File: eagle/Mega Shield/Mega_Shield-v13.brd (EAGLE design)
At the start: 101.6 x 53.3 mm, 27 parts, among them U1 LCD-16X2SILK, U2 LCD-16X2SILK, U3 MAX232PTH

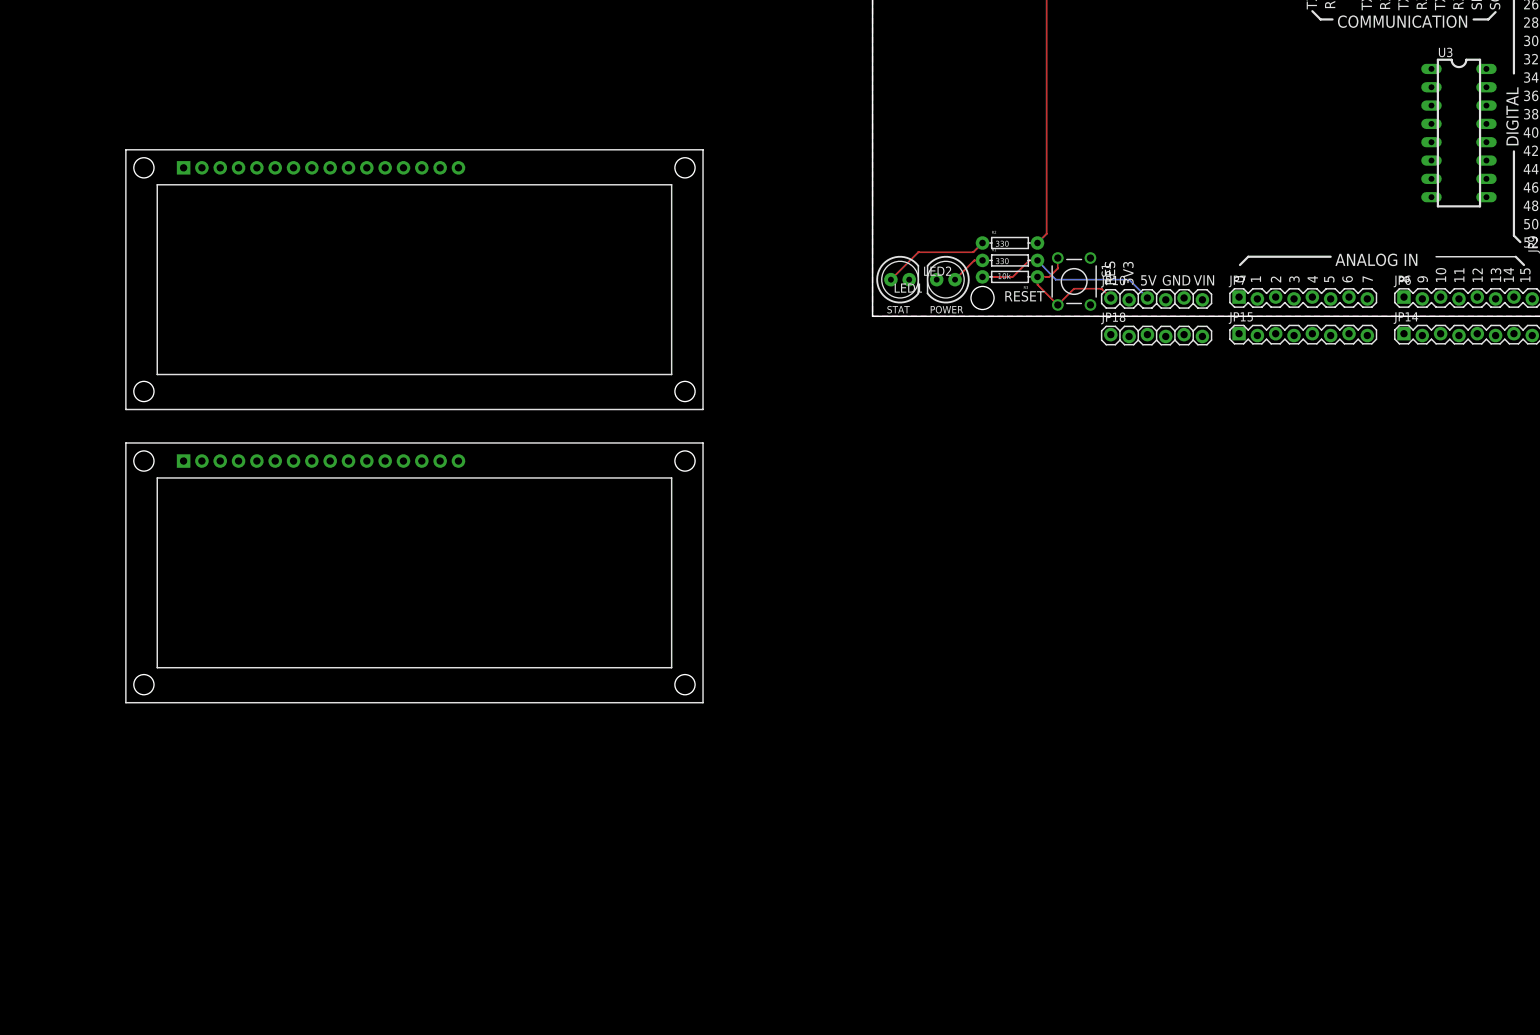
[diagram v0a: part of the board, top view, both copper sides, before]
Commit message: working on pcb, added main connector and lcds
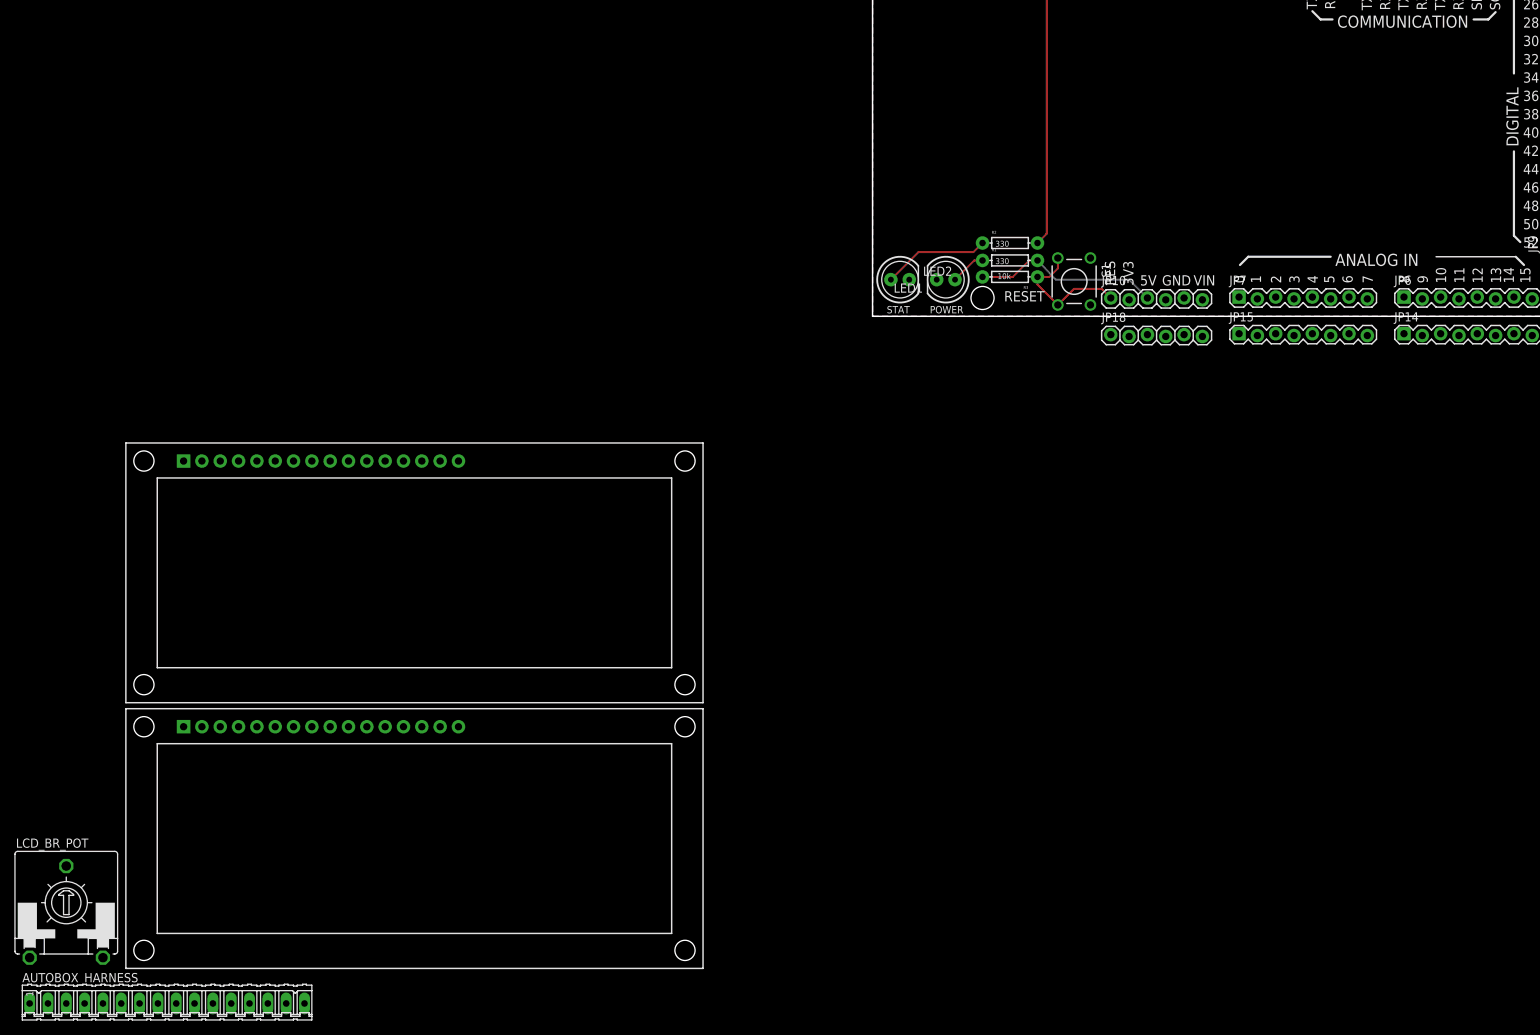
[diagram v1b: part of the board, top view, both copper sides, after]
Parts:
- removed U1: LCD-16X2SILK, SparkFun-Displays:LCD-16X2
- removed U3: MAX232PTH, SparkFun-DigitalIC:DIL16
- added AUTOBOX_HARNESS: (no value), con-amp-quick:16P
- added LCD_1: LCD-16X2SILK, SparkFun-Displays:LCD-16X2
- added LCD_BR_POT: (no value), pot:CA14V
- renumbered U2 to LCD_0
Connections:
- removed net VDD: LCD_0.2, U1.2
- removed net VSS: LCD_0.1, U1.1
- new net LCD_BR: LCD_0.3, LCD_1.3, LCD_BR_POT.S
- new net MODE0: AUTOBOX_HARNESS.8
- new net MODE1: AUTOBOX_HARNESS.9
- new net N$1: AUTOBOX_HARNESS.16
- new net N$2: AUTOBOX_HARNESS.15
- new net SERIAL_K: AUTOBOX_HARNESS.3
- new net SERIAL_L: AUTOBOX_HARNESS.4
- new net SHFT_D: AUTOBOX_HARNESS.14
- new net SHFT_U: AUTOBOX_HARNESS.13
- new net SW1: AUTOBOX_HARNESS.5
- new net SW2: AUTOBOX_HARNESS.6
- new net SW3: AUTOBOX_HARNESS.7
- new net TRC_POT: AUTOBOX_HARNESS.12
- new net TRC_SW0: AUTOBOX_HARNESS.10
- new net TRC_SW1: AUTOBOX_HARNESS.11
- net 5V: now also LCD_0.2, LCD_1.2, LCD_BR_POT.E
- net A: now also LCD_1.15; no longer U1.15
- net D22: now also LCD_0.4
- net D23: now also LCD_0.6
- net D24: now also LCD_0.11
- net D25: now also LCD_0.12
- net D26: now also LCD_0.13
- net D27: now also LCD_0.14
- net D28: now also LCD_1.4
- net D29: now also LCD_1.6
- net D30: now also LCD_1.11
- net D31: now also LCD_1.12
- net D32: now also LCD_1.13
- net D33: now also LCD_1.14
- net GND: now also AUTOBOX_HARNESS.2, LCD_0.1, LCD_0.5, LCD_1.1, LCD_1.5, LCD_BR_POT.A
- net K: now also LCD_1.16; no longer U1.16
- net VIN: now also AUTOBOX_HARNESS.1

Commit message: more changes
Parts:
- added LED3: (no value), led:LED5MM
- added Q1, Q2, Q4: 2N3904, transistor-npn:TO92
- added Q5: 2N3906, transistor-pnp:TO92
- added R10, R4, R6, R8: 10k, SparkFun-Passives:AXIAL-0.3EZ
- added R5, R7, R9: 1k, SparkFun-Passives:AXIAL-0.3EZ
- moved LCD_BR_POT 263.2 mm to (132.1, 17.8), turned to 270 degrees
- moved LCD_1 199.2 mm to (125.7, -10.2)
- moved AUTOBOX_HARNESS 174.5 mm to (5.08, 45.7), turned to 90 degrees
- moved LED1 129.3 mm to (118.1, 76.2), turned to 270 degrees
- moved R1 123.4 mm to (118.5, 80.8), turned to 180 degrees
- moved LCD_0 108.4 mm to (41.9, -10.2)
- moved LED2 71.1 mm to (40.1, 66.2)
- moved R2 59.1 mm to (47.0, 62.2)
- moved JP13 27.9 mm to (88.9, 74.9)
- moved JP1 27.9 mm to (62.2, 74.9)
- moved JP14 27.9 mm to (94.0, 16.5)
- moved JP15 27.9 mm to (71.1, 16.5)
- moved JP5 27.9 mm to (88.9, 69.8)
- moved JP6 27.9 mm to (94.0, 21.6)
- moved JP7 27.9 mm to (71.1, 21.6)
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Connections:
- new net N$10: Q4.1, R10.P$1, R8.P$1
- new net N$3: Q1.1, R4.P$1
- new net N$4: Q1.2, R5.P$1
- new net N$5: Q5.1, R5.P$2, R7.P$2
- new net N$6: Q5.2, R6.P$1
- new net N$7: LED3.A, R7.P$1
- new net N$8: Q2.2, R10.P$2
- net 5V: now also JP12.2, R4.P$2, R8.P$2
- net 5V@1: no longer JP12.2
- net D18: now also Q4.2
- net D19: now also Q1.3
- net GND: now also LED3.K, Q2.3, Q4.3
- net SERIAL_K: now also Q2.1, R6.P$2, R9.P$1
- net VIN: now also Q5.3, R9.P$2
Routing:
- net SERIAL_K: track 0.00 -> 146.7 mm
- net VIN: track 0.25 -> 79.0 mm
- net D13: track 43.4 -> 0.00 mm
- net RES: track 18.6 -> 0.00 mm
- net 5V: track 26.0 -> 7.80 mm
- net N$127: track 14.8 -> 0.00 mm
- net D29: track 0.00 -> 11.3 mm
- net D40: track 0.00 -> 11.3 mm
- net D36: track 0.00 -> 11.3 mm
- net D24: track 0.00 -> 11.3 mm
- net D52: track 0.00 -> 11.3 mm
- net D48: track 0.00 -> 11.3 mm
- net D44: track 0.00 -> 11.3 mm
- net D32: track 0.00 -> 11.3 mm
- net D28: track 0.00 -> 11.3 mm
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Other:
- board size 101.6 x 53.3 mm -> 143.5 x 95.2 mm
- board text added: "K - TX/RX"
- board text added: "LCD_0"
- board text added: "LCD_1"
- board text added: "LCD_BRIGHT"

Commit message: did a lot of pcb work
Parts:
- removed AUTOBOX_HARNESS: (no value), con-amp-quick:16P
- added ABOX_HARN, DSW_LG: (no value), Molex connectors:172064-0012
- added ABOX_PWR, DSW_SM, STEER: (no value), Molex connectors:172064-0004
- added CD4504BE: (no value), ic-package:SOCKET-16
- LCD_0, LCD_1: value LCD-16X2SILK -> 057-010-1; device SparkFun-Displays:LCD-16X2 -> con-panduit:057-010-1
- moved LCD_0 90.0 mm to (119.4, 35.6), turned to 270 degrees
- moved LCD_1 66.3 mm to (119.4, 55.9), turned to 270 degrees
- moved R4 65.9 mm to (68.6, 41.9)
- moved R1 64.8 mm to (68.6, 39.5), turned to 0 degrees
- moved R8 62.0 mm to (68.6, 44.5)
- moved LED1 61.3 mm to (73.3, 34.4), turned to 180 degrees
- moved R10 58.4 mm to (68.6, 47.0), turned to 0 degrees
- moved R6 55.0 mm to (68.6, 49.5), turned to 180 degrees
- moved LCD_BR_POT 50.4 mm to (84.5, 34.2), turned to 0 degrees
- moved Q4 49.0 mm to (68.6, 54.6), turned to 180 degrees
- moved LED3 47.3 mm to (77.5, 47.0), turned to 180 degrees
- moved R5 45.9 mm to (87.6, 44.5), turned to 0 degrees
- moved R7 40.8 mm to (87.6, 47.0), turned to 0 degrees
- moved Q2 38.7 mm to (74.9, 54.6), turned to 180 degrees
- moved R9 35.8 mm to (87.6, 49.5), turned to 0 degrees
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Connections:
- removed net 5V@1: JP12.1
- removed net A: LCD_0.15, LCD_1.15
- removed net K: LCD_0.16, LCD_1.16
- removed net N$3: Q1.1, R4.P$1
- new net N$11: CD4504BE.2
- new net N$12: CD4504BE.3
- new net N$13: CD4504BE.4
- new net N$14: CD4504BE.5
- new net N$15: CD4504BE.6
- new net N$16: CD4504BE.7
- new net N$19: CD4504BE.15
- new net N$20: CD4504BE.14
- new net N$22: CD4504BE.12
- new net N$23: CD4504BE.11
- new net N$24: CD4504BE.10
- new net N$25: CD4504BE.9
- net 5V: now also CD4504BE.1, JP12.1, LCD_0.3, LCD_1.3; no longer LCD_0.2, LCD_1.2
- net D19: now also Q1.1, R4.P$1; no longer Q1.3
- net D22: now also LCD_0.7; no longer LCD_0.4
- net D23: now also LCD_0.2; no longer LCD_0.6
- net D24: now also LCD_0.4; no longer LCD_0.11
- net D25: now also LCD_0.6; no longer LCD_0.12
- net D26: now also LCD_0.8; no longer LCD_0.13
- net D27: now also LCD_0.10; no longer LCD_0.14
- net D28: now also LCD_1.7; no longer LCD_1.4
- net D29: now also LCD_1.2; no longer LCD_1.6
- net D30: now also LCD_1.4; no longer LCD_1.11
- net D31: now also LCD_1.6; no longer LCD_1.12
- net D32: now also LCD_1.8; no longer LCD_1.13
- net D33: now also LCD_1.10; no longer LCD_1.14
- net GND: now also ABOX_PWR.CKT2, CD4504BE.13, CD4504BE.8, LCD_0.9, LCD_1.9, Q1.3; no longer AUTOBOX_HARNESS.2, LCD_0.5, LCD_1.5
- net LCD_BR: now also LCD_0.5, LCD_1.5; no longer LCD_0.3, LCD_1.3
- net MODE0: now also ABOX_HARN.CKT6; no longer AUTOBOX_HARNESS.8
- net MODE1: now also ABOX_HARN.CKT7; no longer AUTOBOX_HARNESS.9
- net N$1: now also ABOX_HARN.CKT12; no longer AUTOBOX_HARNESS.16
- net N$2: now also ABOX_HARN.CKT11; no longer AUTOBOX_HARNESS.15
- net SERIAL_K: now also ABOX_HARN.CKT1; no longer AUTOBOX_HARNESS.3
- net SERIAL_L: now also ABOX_HARN.CKT2; no longer AUTOBOX_HARNESS.4
- net SHFT_D: now also ABOX_PWR.CKT4; no longer AUTOBOX_HARNESS.14
- net SHFT_U: now also ABOX_PWR.CKT3; no longer AUTOBOX_HARNESS.13
- net SW1: now also ABOX_HARN.CKT3; no longer AUTOBOX_HARNESS.5
- net SW2: now also ABOX_HARN.CKT4; no longer AUTOBOX_HARNESS.6
- net SW3: now also ABOX_HARN.CKT5; no longer AUTOBOX_HARNESS.7
- net TRC_POT: now also ABOX_HARN.CKT10; no longer AUTOBOX_HARNESS.12
- net TRC_SW0: now also ABOX_HARN.CKT8; no longer AUTOBOX_HARNESS.10
- net TRC_SW1: now also ABOX_HARN.CKT9; no longer AUTOBOX_HARNESS.11
- net VIN: now also ABOX_PWR.CKT1, CD4504BE.16; no longer AUTOBOX_HARNESS.1
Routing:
- net 5V: track 7.80 -> 292.4 mm, vias 0 -> 1
- net VIN: track 79.0 -> 230.4 mm
- net LCD_BR: track 0.00 -> 84.1 mm, vias 0 -> 4
- net SERIAL_K: track 146.7 -> 66.1 mm
- net D27: track 11.2 -> 64.7 mm, vias 0 -> 1
- net D25: track 11.2 -> 64.0 mm, vias 0 -> 2
- net D19: track 0.13 -> 45.9 mm
- net D23: track 11.2 -> 56.8 mm, vias 0 -> 2
- net D18: track 0.13 -> 38.8 mm
- net D30: track 11.2 -> 45.9 mm
- net D13: track 0.00 -> 31.7 mm
- net D28: track 11.3 -> 40.2 mm, vias 0 -> 2
- net D32: track 11.3 -> 37.0 mm
- net D24: track 11.3 -> 36.9 mm
- net N$10: track 0.00 -> 16.8 mm
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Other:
- board size 143.5 x 95.2 mm -> 119.4 x 91.4 mm
- board text added: "AUTOBOX HARNESS"
- board text added: "AUTOBOX POWER"
- board text added: "DSW_LG"
- board text added: "DSW_SM"
- board text added: "STEER"

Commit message: lots of board work
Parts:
- removed LCD_BR_POT: (no value), pot:CA14V
- added CD4504BE1: (no value), ic-package:SOCKET-16
- added R11: (no value), pot:CT6
- added R12, R13, R14, R15, R16: 10k, SparkFun-Passives:AXIAL-0.3EZ
- moved ABOX_PWR 136.8 mm to (6.35, 29.2), turned to 270 degrees
- moved R1 47.5 mm to (32.0, 9.14), turned to 270 degrees
- moved LCD_1 46.3 mm to (90.2, 19.9), turned to 180 degrees
- moved LED1 38.6 mm to (39.2, 16.1), turned to 270 degrees
- moved R4 32.2 mm to (100.5, 46.4), turned to 270 degrees
- moved ABOX_HARN 31.1 mm to (102.9, 130.8)
- moved DSW_LG 31.1 mm to (52.1, 130.8)
- moved DSW_SM 31.1 mm to (66.0, 130.8)
- moved STEER 31.1 mm to (15.2, 130.8)
- moved JP9 30.2 mm to (106.7, 55.9), turned to 270 degrees
- moved LCD_0 30.0 mm to (90.2, 28.6), turned to 180 degrees
- moved JP17 29.6 mm to (114.3, 55.9), turned to 270 degrees
- moved JP12 11.7 mm to (106.7, 58.4)
- moved JP13 11.7 mm to (81.3, 63.5)
- moved JP14 11.7 mm to (86.4, 5.08)
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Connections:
- removed net N$1: ABOX_HARN.CKT12
- removed net N$11: CD4504BE.2
- removed net N$12: CD4504BE.3
- removed net N$13: CD4504BE.4
- removed net N$14: CD4504BE.5
- removed net N$15: CD4504BE.6
- removed net N$16: CD4504BE.7
- removed net N$2 (its old number): ABOX_HARN.CKT11
- removed net N$24: CD4504BE.10
- removed net N$25: CD4504BE.9
- removed net TRC_POT: ABOX_HARN.CKT10
- removed net TRC_SW0: ABOX_HARN.CKT8
- removed net TRC_SW1: ABOX_HARN.CKT9
- new net LAUNCHSW_12: CD4504BE.3, DSW_LG.CKT2, R13.P$2
- new net LAUNCHSW_LED: CD4504BE1.2, DSW_LG.CKT3
- new net LAUNCH_LED: ABOX_HARN.CKT11, CD4504BE1.3
- new net LAUNCH_SW: ABOX_HARN.CKT8, CD4504BE.2
- new net N$27: CD4504BE1.6
- new net N$28: CD4504BE1.7
- new net N$29: DSW_SM.CKT4
- new net N$32: CD4504BE1.15
- new net N$33: CD4504BE1.14
- new net N$35: CD4504BE1.12
- new net N$36: CD4504BE1.11
- new net N$37: CD4504BE1.10
- new net N$38: CD4504BE1.9
- new net N$97: DSW_SM.CKT3
- new net N$98: DSW_SM.CKT2
- new net N$99: DSW_SM.CKT1
- new net TRAC_LED: ABOX_HARN.CKT12, CD4504BE1.5
- new net TRA_CTL_LED: CD4504BE1.4, DSW_LG.CKT5
- new net TRA_CTL_POT: ABOX_HARN.CKT10, DSW_LG.CKT7
- new net TRA_CTL_SW: ABOX_HARN.CKT9, CD4504BE.4
- new net TRA_CTL_SW_12: CD4504BE.5, DSW_LG.CKT4, R14.P$2
- net 5V: now also CD4504BE.16, CD4504BE1.1, R11.E, R12.P$1; no longer CD4504BE.1, LCD_BR_POT.E
- net D22: now also CD4504BE.6; no longer LCD_0.7
- net D23: now also CD4504BE.10; no longer LCD_0.2
- net D24: now also DSW_LG.CKT6, R12.P$2; no longer LCD_0.4
- net D25: no longer LCD_0.6
- net D26: no longer LCD_0.8
- net D27: no longer LCD_0.10
- net D28: no longer LCD_1.7
- net D29: no longer LCD_1.2
- net D30: no longer LCD_1.4
- net D31: no longer LCD_1.6
- net D32: no longer LCD_1.8
- net D33: no longer LCD_1.10
- net D42: now also LCD_0.7
- net D43: now also LCD_0.2
- net D44: now also LCD_0.4
- net D45: now also LCD_0.6
- net D46: now also LCD_0.8
- net D47: now also LCD_0.10
- net D48: now also LCD_1.7
- net D49: now also LCD_1.2
- net D50: now also LCD_1.4
- net D51: now also LCD_1.6
- net D52: now also LCD_1.8
- net D53: now also LCD_1.10
- net GND: now also CD4504BE1.13, CD4504BE1.8, R11.A, R13.P$1, R14.P$1, R15.P$2, R16.P$1, STEER.CKT2; no longer LCD_BR_POT.A
- net LCD_BR: now also R11.S; no longer LCD_BR_POT.S
- net MODE0: now also DSW_LG.CKT8
- net MODE1: now also DSW_LG.CKT9
- net SHFT_D: now also CD4504BE.9, R16.P$2, STEER.CKT4
- net SHFT_U: now also CD4504BE.7, R15.P$1, STEER.CKT3
- net SW1: now also DSW_LG.CKT10
- net SW2: now also DSW_LG.CKT11
- net SW3: now also DSW_LG.CKT12
- net VIN: now also CD4504BE.1, CD4504BE1.16, DSW_LG.CKT1, STEER.CKT1; no longer CD4504BE.16
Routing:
- net VIN: track 230.4 -> 11.2 mm
- net D27: track 64.7 -> 8.67 mm, vias 1 -> 0
- net D25: track 64.0 -> 8.67 mm, vias 2 -> 0
- net LCD_BR: track 84.1 -> 29.6 mm, vias 4 -> 0
- net 5V: track 292.4 -> 243.4 mm
- net D23: track 56.8 -> 8.67 mm, vias 2 -> 0
- net D30: track 45.9 -> 8.75 mm
- net D28: track 40.2 -> 8.67 mm, vias 2 -> 0
- net D32: track 37.0 -> 8.67 mm
- net D24: track 36.9 -> 8.55 mm
- net D47: track 11.2 -> 35.9 mm, vias 0 -> 1
- net D53: track 11.2 -> 34.7 mm, vias 0 -> 1
- net D46: track 11.2 -> 29.9 mm
- net D42: track 11.2 -> 29.6 mm
- net D51: track 11.2 -> 29.5 mm, vias 0 -> 1
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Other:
- board size 119.4 x 91.4 mm -> 113 x 96.5 mm
- board text removed: "LCD_0"
- board text removed: "LCD_1"
